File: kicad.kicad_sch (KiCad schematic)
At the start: 0 parts

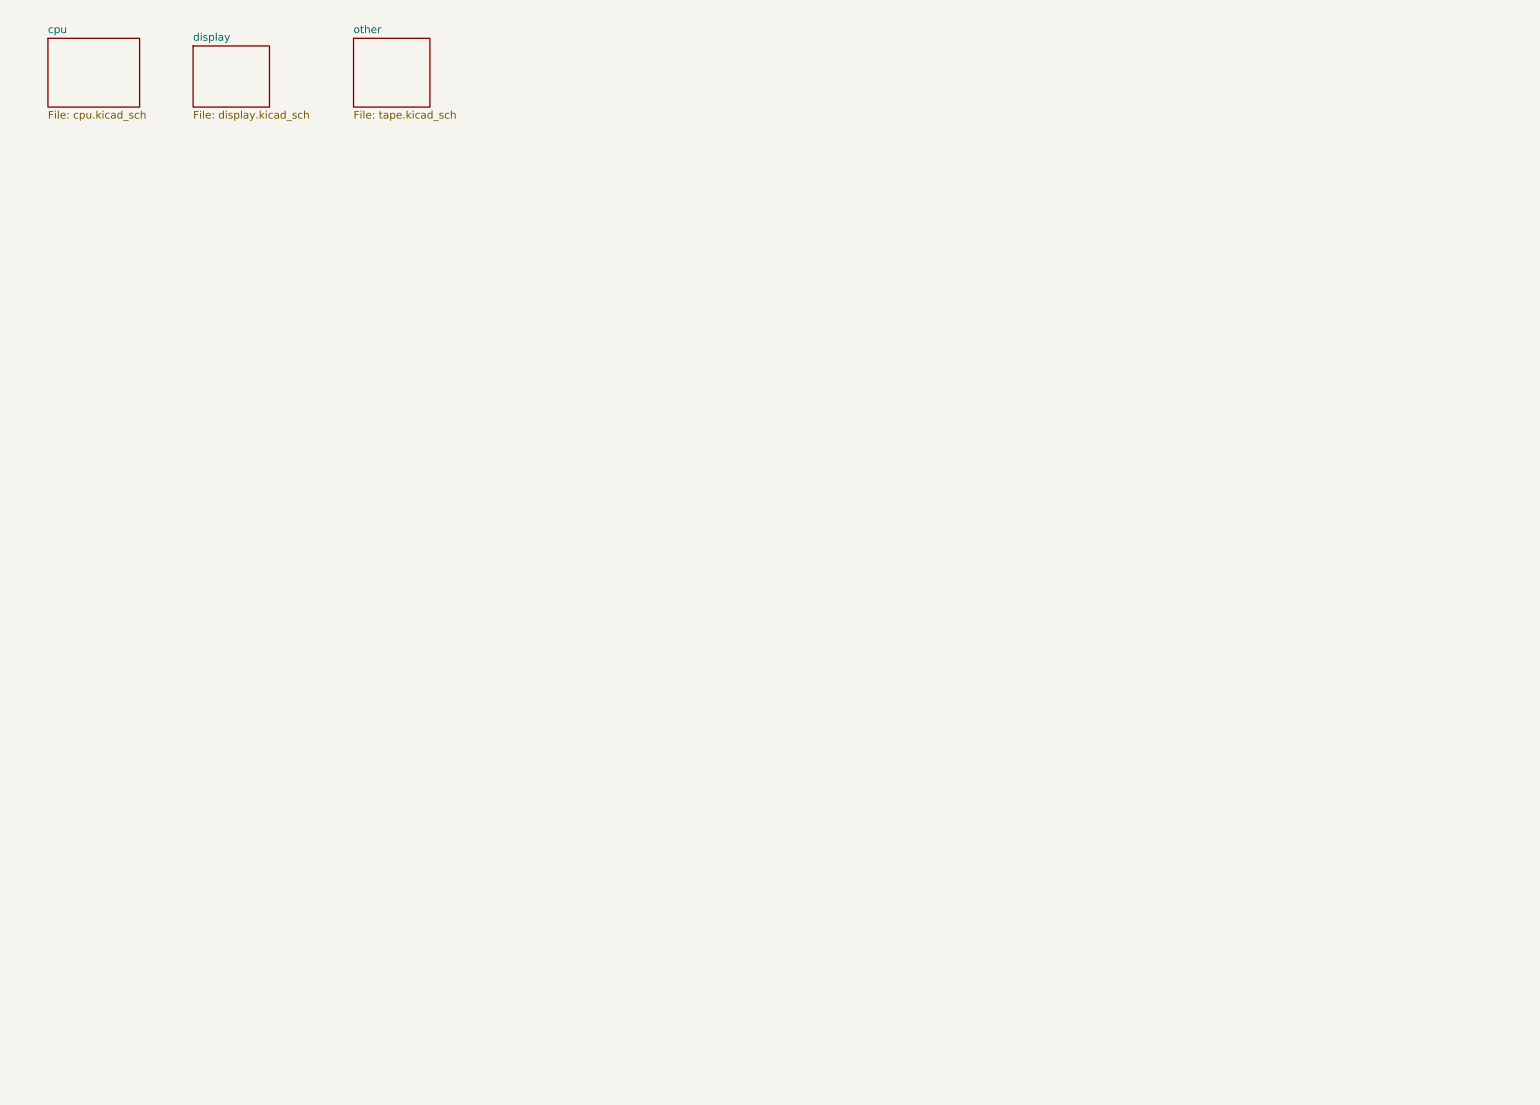
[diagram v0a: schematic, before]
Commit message: full rework. ic numbers now same as in original schema
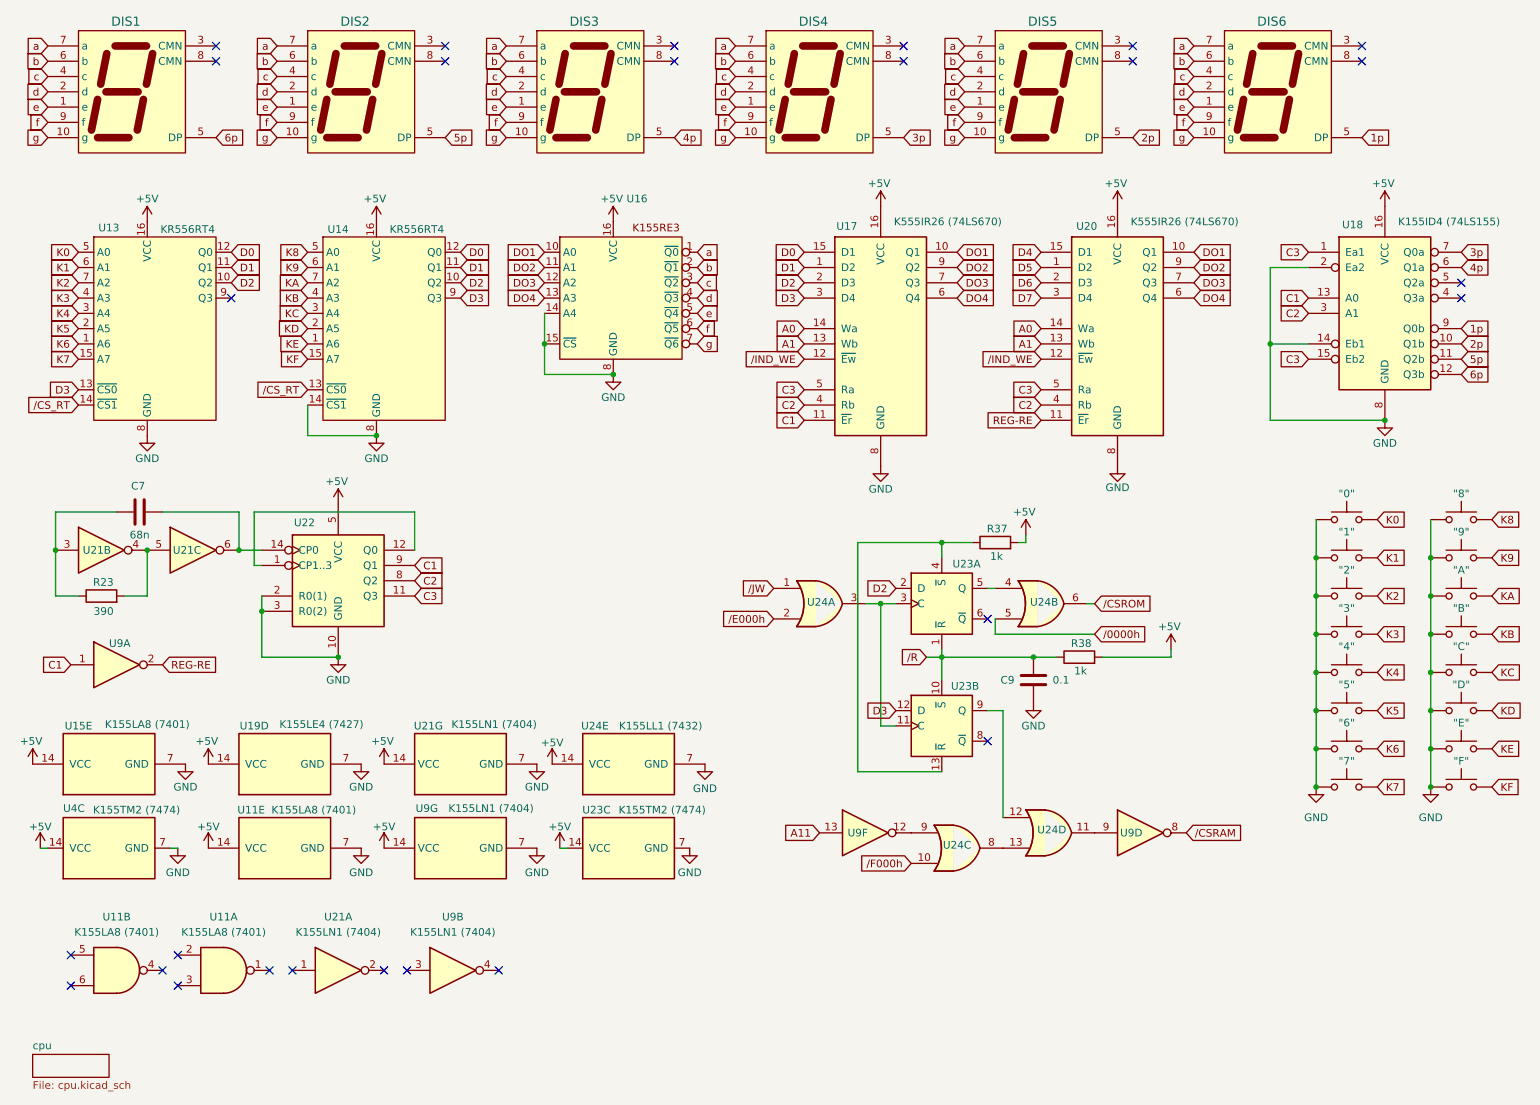
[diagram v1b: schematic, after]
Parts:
- added C7: 68n, Capacitor_THT:C_Radial_D5.0mm_H5.0mm_P2.00mm, symbol Device:C
- added C9: 0.1, Capacitor_THT:C_Radial_D5.0mm_H5.0mm_P2.00mm, symbol Device:C
- added DIS1, DIS2, DIS3, DIS4, DIS5, DIS6: HDSP-5503, symbol User:HDSP-5503
- added R23: 390, Resistor_THT:R_Axial_DIN0204_L3.6mm_D1.6mm_P5.08mm_Horizontal, symbol Device:R
- added R37, R38: 1k, Resistor_THT:R_Axial_DIN0204_L3.6mm_D1.6mm_P5.08mm_Horizontal, symbol Device:R
- added SW10: "7", symbol Switch:SW_Push
- added SW11: "8", symbol Switch:SW_Push
- added SW12: "9", symbol Switch:SW_Push
- added SW13: "A", symbol Switch:SW_Push
- added SW14: "B", symbol Switch:SW_Push
- added SW15: "C", symbol Switch:SW_Push
- added SW16: "D", symbol Switch:SW_Push
- added SW17: "E", symbol Switch:SW_Push
- added SW18: "F", symbol Switch:SW_Push
- added SW3: "0", symbol Switch:SW_Push
- added SW4: "1", symbol Switch:SW_Push
- added SW5: "2", symbol Switch:SW_Push
- added SW6: "3", symbol Switch:SW_Push
- added SW7: "4", symbol Switch:SW_Push
- added SW8: "5", symbol Switch:SW_Push
- added SW9: "6", symbol Switch:SW_Push
- added U11, U15: K155LA8 (7401), Package_DIP:DIP-14_W7.62mm, symbol 74xx:74LS01
- added U13, U14: KR556RT4, Package_DIP:DIP-16_W7.62mm_LongPads, symbol User:kr556rt4
- added U16: ~, symbol User:k155re3
- added U17, U20: K555IR26 (74LS670), Package_DIP:DIP-16_W7.62mm_LongPads, symbol 74xx:74LS670
- added U18: K155ID4 (74LS155), Package_DIP:DIP-16_W7.62mm_LongPads, symbol 74xx:74LS155
- added U19: K155LE4 (7427), Package_DIP:DIP-14_W7.62mm, symbol 74xx:74LS27
- added U21: K155LN1 (7404), Package_DIP:DIP-14_W7.62mm_LongPads, symbol 74xx:74LS04
- added U22: K155IE5 (7493), symbol 74xx:74LS93
- added U23: K155TM2 (7474), Package_DIP:DIP-14_W7.62mm_LongPads, symbol 74xx:74LS74
- added U24: K155LL1 (7432), Package_DIP:DIP-14_W7.62mm_LongPads, symbol 74xx:74LS32
- added U4: K155TM2 (7474), Package_DIP:DIP-14_W7.62mm, symbol 74xx:74LS74
- added U9: K155LN1 (7404), Package_DIP:DIP-14_W7.62mm, symbol 74xx:74LS04
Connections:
- new net: C7.1, R23.1, U21.3
- new net: C7.2, U21.6, U22.14 (CP0)
- new net: U23.11 (C), U23.3 (C), U24.3
- new net: R37.1, U23.13 (~{R}), U23.4 (~{S})
- new net: U23.9 (Q), U24.12
- new net: R23.2, U21.4, U21.5
- new net: U24.13, U24.8
- new net: U24.9, U9.12
- new net: U23.5 (Q), U24.4
- new net: U24.11, U9.9
- new net: U22.1 (CP1..3), U22.12 (Q0)
- new net +5V: R37.2, R38.2, U11.14 (VCC), U13.16 (VCC), U14.16 (VCC), U15.14 (VCC), U16.16 (VCC), U17.16 (VCC), U18.16 (VCC), U19.14 (VCC), U20.16 (VCC), U21.14 (VCC), U22.5 (VCC), U23.14 (VCC), U24.14 (VCC), U4.14 (VCC), U9.14 (VCC)
- new net 1p: DIS6.5 (DP), U18.9 (Q0b)
- new net 2p: DIS5.5 (DP), U18.10 (Q1b)
- new net 3p: DIS4.5 (DP), U18.7 (Q0a)
- new net 4p: DIS3.5 (DP), U18.6 (Q1a)
- new net 5p: DIS2.5 (DP), U18.11 (Q2b)
- new net 6p: DIS1.5 (DP), U18.12 (Q3b)
- new net A0: U17.14 (Wa), U20.14 (Wa)
- new net A1: U17.13 (Wb), U20.13 (Wb)
- new net A11: U9.13
- new net C1: U17.11 (~{Er}), U18.13 (A0), U22.9 (Q1), U9.1
- new net C2: U17.4 (Rb), U18.3 (A1), U20.4 (Rb), U22.8 (Q2)
- new net C3: U17.5 (Ra), U18.1 (Ea1), U18.15 (Eb2), U20.5 (Ra), U22.11 (Q3)
- new net D0: U13.12 (Q0), U14.12 (Q0), U17.15 (D1)
- new net D1: U13.11 (Q1), U14.11 (Q1), U17.1 (D2)
- new net D2: U13.10 (Q2), U14.10 (Q2), U17.2 (D3), U23.2 (D)
- new net D3: U13.13 (~{CS0}), U14.9 (Q3), U17.3 (D4), U23.12 (D)
- new net D4: U20.15 (D1)
- new net D5: U20.1 (D2)
- new net D6: U20.2 (D3)
- new net D7: U20.3 (D4)
- new net DO1: U16.10 (A0), U17.10 (Q1), U20.10 (Q1)
- new net DO2: U16.11 (A1), U17.9 (Q2), U20.9 (Q2)
- new net DO3: U16.12 (A2), U17.7 (Q3), U20.7 (Q3)
- new net DO4: U16.13 (A3), U17.6 (Q4), U20.6 (Q4)
- new net GND: C9.1, SW10.1, SW11.1, SW12.1, SW13.1, SW14.1, SW15.1, SW16.1, SW17.1, SW18.1, SW3.1, SW4.1, SW5.1, SW6.1, SW7.1, SW8.1, SW9.1, U11.7 (GND), U13.8 (GND), U14.14 (~{CS1}), U14.8 (GND), U15.7 (GND), U16.14 (A4), U16.15 (~{CS}), U16.8 (GND), U17.8 (GND), U18.14 (Eb1), U18.2 (Ea2), U18.8 (GND), U19.7 (GND), U20.8 (GND), U21.7 (GND), U22.10 (GND), U22.2 (R0(1)), U22.3 (R0(2)), U23.7 (GND), U24.7 (GND), U4.7 (GND), U9.7 (GND)
- new net K0: SW3.2, U13.5 (A0)
- new net K1: SW4.2, U13.6 (A1)
- new net K2: SW5.2, U13.7 (A2)
- new net K3: SW6.2, U13.4 (A3)
- new net K4: SW7.2, U13.3 (A4)
- new net K5: SW8.2, U13.2 (A5)
- new net K6: SW9.2, U13.1 (A6)
- new net K7: SW10.2, U13.15 (A7)
- new net K8: SW11.2, U14.5 (A0)
- new net K9: SW12.2, U14.6 (A1)
- new net KA: SW13.2, U14.7 (A2)
- new net KB: SW14.2, U14.4 (A3)
- new net KC: SW15.2, U14.3 (A4)
- new net KD: SW16.2, U14.2 (A5)
- new net KE: SW17.2, U14.1 (A6)
- new net KF: SW18.2, U14.15 (A7)
- new net REG-RE: U20.11 (~{Er}), U9.2
- new net a: DIS1.7 (a), DIS2.7 (a), DIS3.7 (a), DIS4.7 (a), DIS5.7 (a), DIS6.7 (a), U16.1 (~{Q0})
- new net b: DIS1.6 (b), DIS2.6 (b), DIS3.6 (b), DIS4.6 (b), DIS5.6 (b), DIS6.6 (b), U16.2 (~{Q1})
- new net c: DIS1.4 (c), DIS2.4 (c), DIS3.4 (c), DIS4.4 (c), DIS5.4 (c), DIS6.4 (c), U16.3 (~{Q2})
- new net d: DIS1.2 (d), DIS2.2 (d), DIS3.2 (d), DIS4.2 (d), DIS5.2 (d), DIS6.2 (d), U16.4 (~{Q3})
- new net e: DIS1.1 (e), DIS2.1 (e), DIS3.1 (e), DIS4.1 (e), DIS5.1 (e), DIS6.1 (e), U16.5 (~{Q4})
- new net f: DIS1.9 (f), DIS2.9 (f), DIS3.9 (f), DIS4.9 (f), DIS5.9 (f), DIS6.9 (f), U16.6 (~{Q5})
- new net g: DIS1.10 (g), DIS2.10 (g), DIS3.10 (g), DIS4.10 (g), DIS5.10 (g), DIS6.10 (g), U16.7 (~{Q6})
- new net /0000h: U24.5
- new net /CSRAM: U9.8
- new net /CSROM: U24.6
- new net /CS_RT: U13.14 (~{CS1}), U14.13 (~{CS0})
- new net /E000h: U24.2
- new net /F000h: U24.10
- new net /IND_WE: U17.12 (~{Ew}), U20.12 (~{Ew})
- new net /JW: U24.1
- new net /R: C9.2, R38.1, U23.1 (~{R}), U23.10 (~{S})
- no-connect marks 0 -> 27
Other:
- removed sheet display
- removed sheet other
- company: Eugene Chertikhin -> (none)
- title: ЮТ-88 mainboard -> (none)

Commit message: footprints
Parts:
- U11, U15: value K155LA8 (7401) -> K155ЛА8; footprint Package_DIP:DIP-14_W7.62mm -> Package_DIP:DIP-14_W7.62mm_LongPads; Analog (none) -> 7401
- U13, U14: value KR556RT4 -> KR556РТ4
- U17, U20: value K555IR26 (74LS670) -> K555ИР26; Analog (none) -> 74LS670
- U18: value K155ID4 (74LS155) -> K155ИД4; Analog (none) -> 74155
- U19: value K155LE4 (7427) -> K155ЛЕ4; footprint Package_DIP:DIP-14_W7.62mm -> Package_DIP:DIP-14_W7.62mm_LongPads; Analog (none) -> 7427
- U21: value K155LN1 (7404) -> K155ЛН1; Analog (none) -> 7404
- U22: value K155IE5 (7493) -> K155ИЕ5; footprint (none) -> Package_DIP:DIP-14_W7.62mm_LongPads; Analog (none) -> 7493
- U23: value K155TM2 (7474) -> K155ТМ2; Analog (none) -> 7474
- U24: value K155LL1 (7432) -> K155ЛЛ1; Analog (none) -> 7432
- U4: value K155TM2 (7474) -> K155ТМ2; footprint Package_DIP:DIP-14_W7.62mm -> Package_DIP:DIP-14_W7.62mm_LongPads; Analog (none) -> 7474
- U9: value K155LN1 (7404) -> K155ЛН1; footprint Package_DIP:DIP-14_W7.62mm -> Package_DIP:DIP-14_W7.62mm_LongPads; Analog (none) -> 7404
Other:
- moved on the sheet: U24C, U9F
